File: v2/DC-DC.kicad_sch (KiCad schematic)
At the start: 71 parts, among them Q1 CSD19534Q5A, SW3 CJS-1200TA, U11 SSF2215, U12 TPS72301DBV, U13 LM5155DSSR, U2 TLV75733PDYDR, U3 TLV75733PDYDR, U4 TPSM84209RKHR, U9 TPS60403DBV

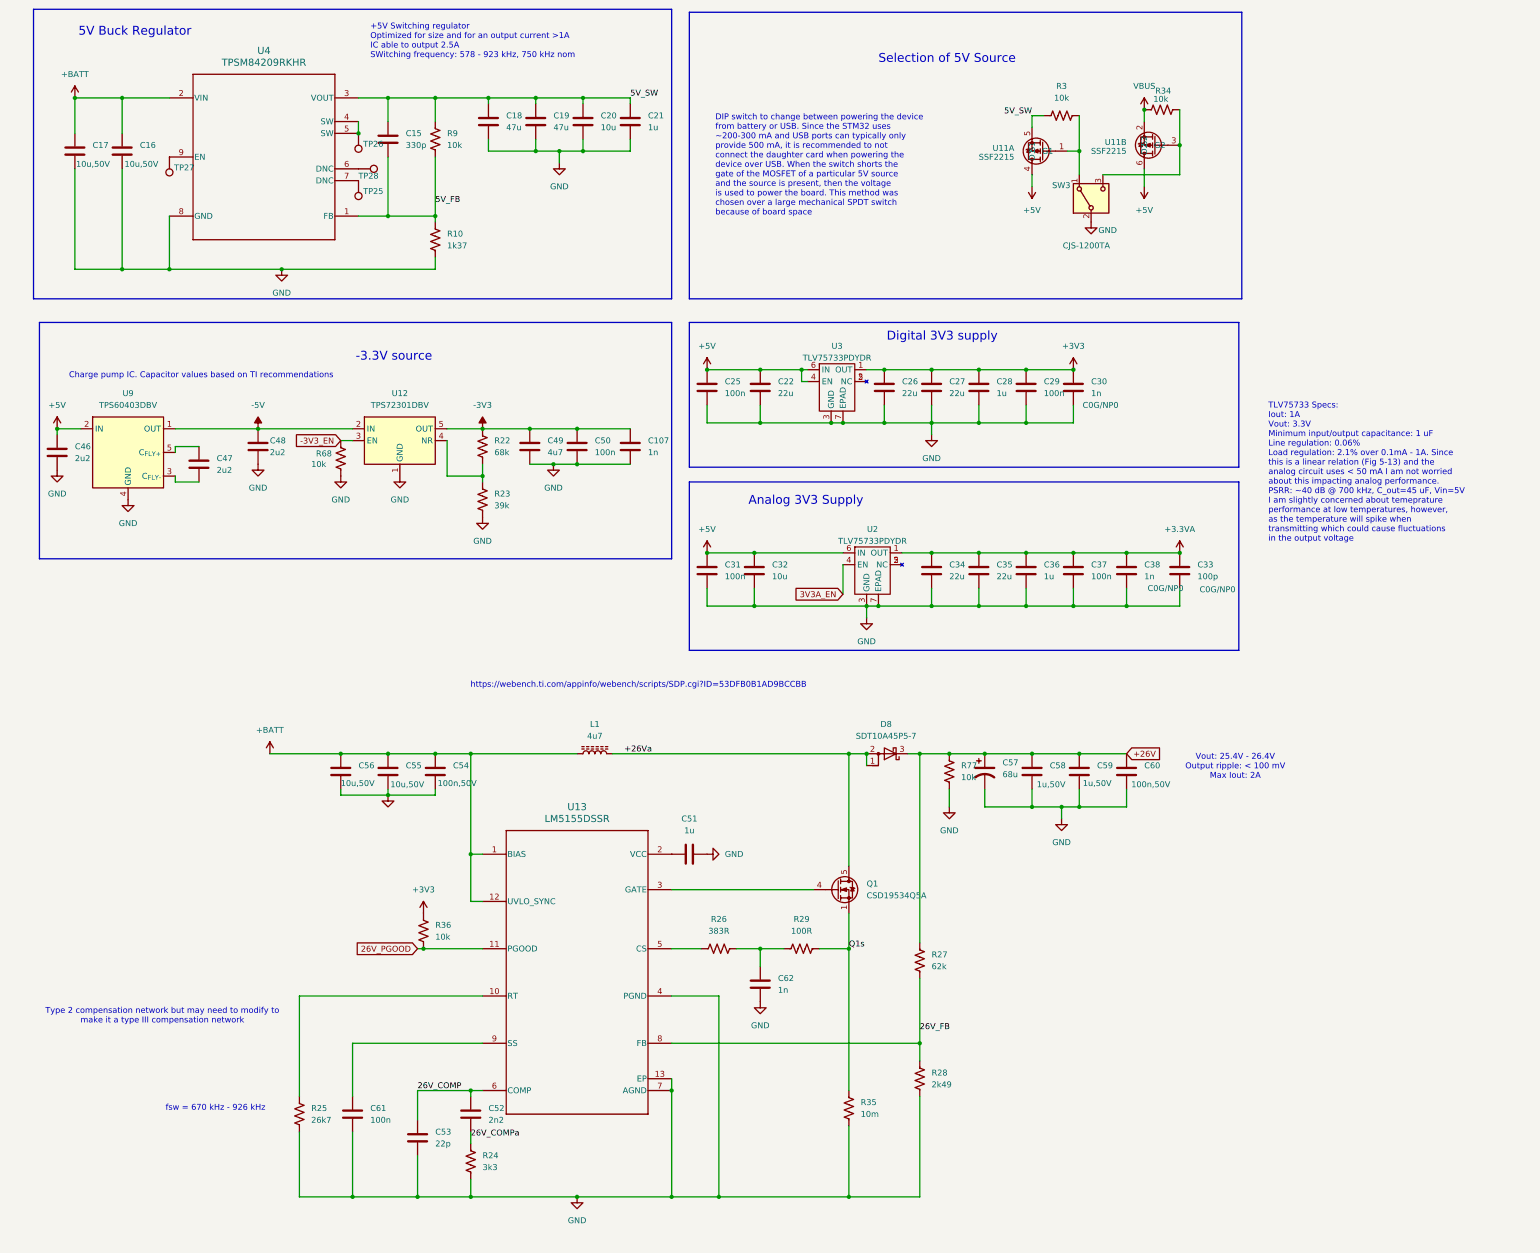
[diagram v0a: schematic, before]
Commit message: Most v2 changes made
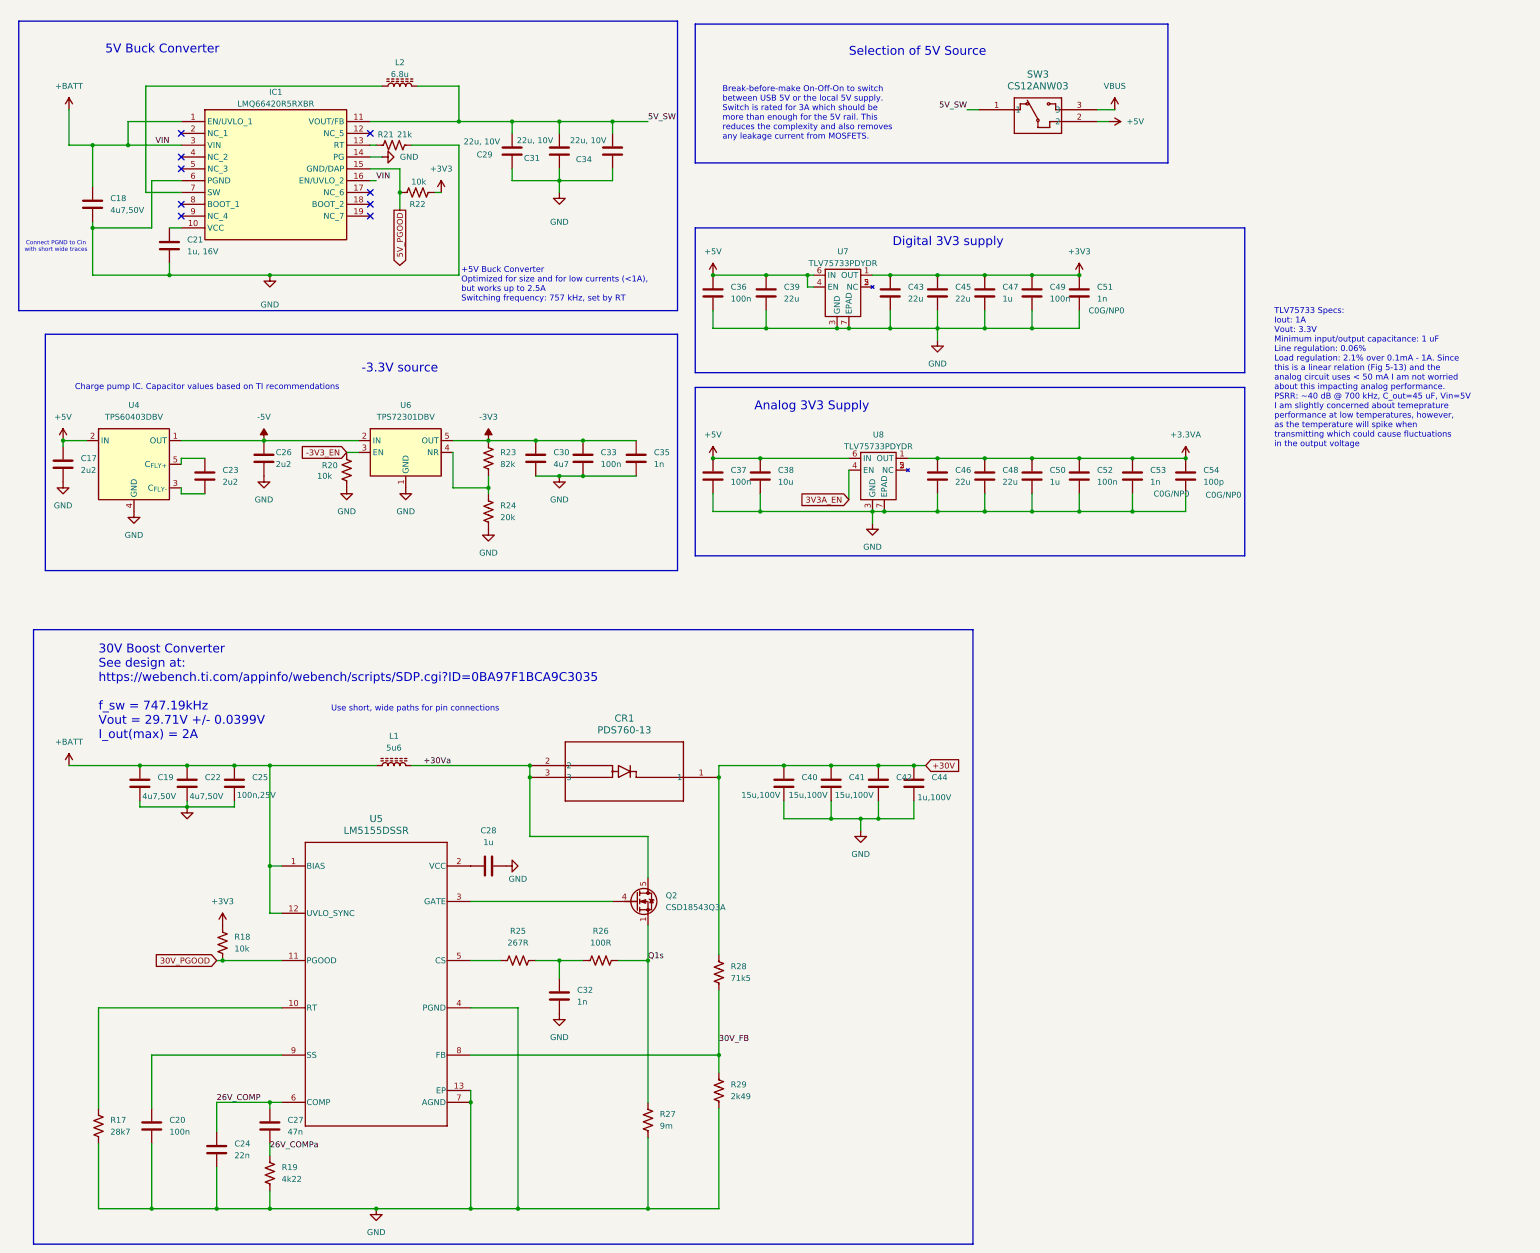
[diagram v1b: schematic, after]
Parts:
- removed C15: 330p, Capacitor_SMD:C_0603_1608Metric_Pad1.08x0.95mm_HandSolder, symbol UAM_symbols:C
- removed C16, C17, C56: 10u,50V, Capacitor_SMD:C_1210_3225Metric_Pad1.33x2.70mm_HandSolder, symbol UAM_symbols:C
- removed C18: 47u, Capacitor_SMD:C_1210_3225Metric_Pad1.33x2.70mm_HandSolder, symbol UAM_symbols:C
- removed C20: 10u, Capacitor_SMD:C_0805_2012Metric_Pad1.18x1.45mm_HandSolder, symbol UAM_symbols:C
- removed C21, C28: 1u, Capacitor_SMD:C_0603_1608Metric_Pad1.08x0.95mm_HandSolder, symbol UAM_symbols:C
- removed C22, C26, C27: 22u, Capacitor_SMD:C_0805_2012Metric_Pad1.18x1.45mm_HandSolder, symbol UAM_symbols:C
- removed C25, C29: 100n, Capacitor_SMD:C_0603_1608Metric_Pad1.08x0.95mm_HandSolder, symbol UAM_symbols:C
- removed C57: 68u, Capacitor_THT:CP_Radial_D6.3mm_P2.50mm, symbol UAM_symbols:C_Polarized_US
- removed C58, C59: 1u,50V, Capacitor_SMD:C_0603_1608Metric_Pad1.08x0.95mm_HandSolder, symbol UAM_symbols:C
- removed C60: 100n,50V, Capacitor_SMD:C_0603_1608Metric_Pad1.08x0.95mm_HandSolder, symbol UAM_symbols:C
- removed D8: SDT10A45P5-7, Diodes:PowerDI-5, symbol UAM_symbols:D_Schottky_AAK
- removed Q1: CSD19534Q5A, Package_TO_SOT_SMD:TDSON-8-1, symbol UAM_symbols:CSD19534Q5A
- removed R10: 1k37, Resistor_SMD:R_0603_1608Metric_Pad0.98x0.95mm_HandSolder, symbol UAM_symbols:R_US
- removed R22: 68k, Resistor_SMD:R_0603_1608Metric_Pad0.98x0.95mm_HandSolder, symbol UAM_symbols:R_US
- removed R25: 26k7, Resistor_SMD:R_0603_1608Metric_Pad0.98x0.95mm_HandSolder, symbol UAM_symbols:R_US
- removed R3, R34, R77, R9: 10k, Resistor_SMD:R_0603_1608Metric_Pad0.98x0.95mm_HandSolder, symbol UAM_symbols:R_US
- removed SW3: CJS-1200TA, Switches:CJS-1200TA, symbol UAM_symbols:SW_SPDT
- removed TP25, TP26, TP27, TP28: ~, TestPoint:TestPoint_Pad_D1.0mm, symbol UAM_symbols:TestPoint
- removed U11: SSF2215, Package_TO_SOT_SMD:SOT-23-6_Handsoldering, symbol UAM_symbols:SSF2215
- removed U2, U3: TLV75733PDYDR, Package_SON:WSON-6-1EP_2x2mm_P0.65mm_EP1x1.6mm, symbol UAM_symbols:TLV75733PDYDR
- removed U4: TPSM84209RKHR, RKH0009A, symbol UAM_symbols:TPSM84209RKHR
- added C18: 4u7,50V, symbol Device:C
- added C21: 1u, 16V, symbol Device:C
- added C29, C31, C34: 22u, 10V, symbol Device:C
- added C36, C49: 100n, Capacitor_SMD:C_0603_1608Metric_Pad1.08x0.95mm_HandSolder, symbol UAM_symbols:C
- added C39, C43, C45: 22u, Capacitor_SMD:C_0805_2012Metric_Pad1.18x1.45mm_HandSolder, symbol UAM_symbols:C
- added C40, C41, C42: 15u,100V, Capacitor_SMD:C_0603_1608Metric_Pad1.08x0.95mm_HandSolder, symbol UAM_symbols:C
- added C44: 1u,100V, Capacitor_SMD:C_0603_1608Metric_Pad1.08x0.95mm_HandSolder, symbol UAM_symbols:C
- added C47: 1u, Capacitor_SMD:C_0603_1608Metric_Pad1.08x0.95mm_HandSolder, symbol UAM_symbols:C
- added CR1: PDS760-13, UAM_footprints:POWERDI5_DIO-M, symbol UAM_symbols:PDS760-13
- added IC1: LMQ66420R5RXBR, UAM_footprints:LMR66430R5RXBR, symbol UAM_symbols:LMQ66420R5RXBR
- added L2: 6.8u, symbol Device:L_Ferrite
- added Q2: CSD18543Q3A, Package_SON:VSON-8_3.3x3.3mm_P0.65mm_NexFET, symbol Transistor_FET:CSD18543Q3A
- added R17: 28k7, Resistor_SMD:R_0603_1608Metric_Pad0.98x0.95mm_HandSolder, symbol UAM_symbols:R_US
- added R19: 4k22, Resistor_SMD:R_0603_1608Metric_Pad0.98x0.95mm_HandSolder, symbol UAM_symbols:R_US
- added R21: 21k, symbol Device:R_US
- added R22: 10k, symbol Device:R_US
- added SW3: CS12ANW03, UAM_footprints:CS12ANW03_NKK, symbol UAM_symbols:CS12ANW03
- added U7, U8: TLV75733PDYDR, Package_SON:WSON-6-1EP_2x2mm_P0.65mm_EP1x1.6mm, symbol UAM_symbols:TLV75733PDYDR
- C19: value 47u -> 4u7,50V
- C22: renamed from C55; value 10u,50V -> 4u7,50V
- C24: renamed from C53; value 22p -> 22n
- C25: renamed from C54; value 100n,50V -> 100n,25V
- C27: renamed from C52; value 2n2 -> 47n
- L1: value 4u7 -> 5u6
- R23: value 39k -> 82k
- R24: value 3k3 -> 20k
- R25: renamed from R26; value 383R -> 267R
- R27: renamed from R35; value 10m -> 9m
- R28: renamed from R27; value 62k -> 71k5
- U5: renamed from U13; footprint DSS0012B -> UAM_footprints:WSON-12-1EP_3x2mm_P0.5mm_EP1x2.65
- renumbered C46 to C17, C61 to C20, C47 to C23, C48 to C26, C51 to C28, C49 to C30, C62 to C32, C50 to C33, C107 to C35, C31 to C37, C32 to C38, C34 to C46, C35 to C48, C36 to C50, C30 to C51, C37 to C52, C38 to C53, C33 to C54, R36 to R18, R68 to R20, R29 to R26, R28 to R29, U9 to U4, U12 to U6
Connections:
- net +3.3VA: now also U8.1 (OUT)
- net +3V3: now also C43.1, C45.1, C47.1, C49.1, R22.2, U7.1 (OUT)
- net +5V: now also C36.1, C39.1, SW3.2, U7.4 (EN), U7.6 (IN), U8.6 (IN)
- net +BATT: now also C19.1, C18.1, IC1.1 (EN/UVLO_1), IC1.16 (EN/UVLO_2), IC1.3 (VIN)
- net -3V3: now also R23.1
- net 26V_COMPa: now also R19.1; no longer R24.1
- net 3V3A_EN: now also U8.4 (EN)
- net 5V_SW: now also C29.1, C31.1, C34.1, IC1.11 (VOUT/FB), L2.2, SW3.1; no longer C19.1
- net GND: now also C18.2, C21.2, C29.2, C31.2, C34.2, C36.2, C39.2, C40.2, C41.2, C42.2, C43.2, C44.2, C45.2, C47.2, C49.2, IC1.14 (PG), IC1.6 (PGND), R17.2, R19.2, R21.2, U7.3 (GND), U7.7 (EPAD), U8.3 (GND), U8.7 (EPAD); no longer R23.2
- net Q1s: now also Q2.1 (S), Q2.2 (S), Q2.3 (S)
- net VBUS: now also SW3.3
- net at U6.4 (NR): now also R23.2, R24.1; no longer R23.1
- net at U5.10 (RT): now also R17.1
- net at U5.3 (GATE): now also Q2.4 (G)
- net +26V renamed +30V
- net +30V: now also C40.1, C41.1, C42.1, C44.1, CR1.1
- net +26Va renamed +30Va
- net +30Va: now also CR1.2, CR1.3, Q2.5 (D)
- net 26V_FB renamed 30V_FB
- net 26V_PGOOD renamed 30V_PGOOD
- new net: C21.1, IC1.10 (VCC)
- new net: IC1.13 (RT), R21.1
- new net: IC1.7 (SW), L2.1
- new net: U8.2 (NC), U8.5 (NC)
- new net: U7.2 (NC), U7.5 (NC)
- new net 5V_PGOOD: IC1.15 (GND/DAP), R22.1
- no-connect marks 0 -> 9
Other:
- note added: "+5V Buck Converter Optimized for size and for low currents (<1A), but works up to 2.5A Switching frequency: 757 kHz, set by RT"
- note added: "30V Boost Converter See design at: https://webench.ti.com/appinfo/webench/scripts/SDP.cgi?ID=0BA97F1BCA9C3035 f_sw = 747.19kHz Vout = 29.71V +/- 0.0399V I_out(max) = 2A"
- note added: "5V Buck Converter"
- note added: "Break-before-make On-Off-On to switch between USB 5V or the local 5V supply. Switch is rated for 3A which should be more than enough for the 5V rail. This reduces the complexity and also removes any leakage current from MOSFETS."
- note added: "Connect PGND to Cin with short wide traces"
- note added: "Use short, wide paths for pin connections"
- note removed: "+5V Switching regulator Optimized for size and for an output current >1A IC able to output 2.5A SWitching frequency: 578 - 923 kHz, 750 kHz nom"
- note removed: "5V Buck Regulator"
- note removed: "DIP switch to change between powering the device from battery or USB. Since the STM32 uses ~200-300 mA and USB ports can typically only provide 500 mA, it is recommended to not connect the daughter card when powering the device over USB. When the switch shorts the gate of the MOSFET of a particular 5V source and the source is present, then the voltage is used to power the board. This method was c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"
- note removed: "Type 2 compensation network but may need to modify to make it a type III compensation network"
- note removed: "Vout: 25.4V - 26.4V Output ripple: < 100 mV Max Iout: 2A"
- note removed: "fsw = 670 kHz - 926 kHz"
- note removed: "https://webench.ti.com/appinfo/webench/scripts/SDP.cgi?ID=53DFB0B1AD9BCCBB"
- company: EV -> (none)
- title: DC-DC conversion -> (none)
- moved on the sheet: C17, C20, C22, C23, C24, C25, C26, C27, C28, C30, C32, C33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
